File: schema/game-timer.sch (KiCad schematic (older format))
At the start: 39 parts, among them IC1 ATMEGA8515-P, SW1 Старт, SW10 Игрок4, SW2 Сброс, SW3 Время1, SW4 Время2, SW5 Время3, SW6 Время4, SW7 Игрок1, SW8 Игрок1, SW9 Игрок3

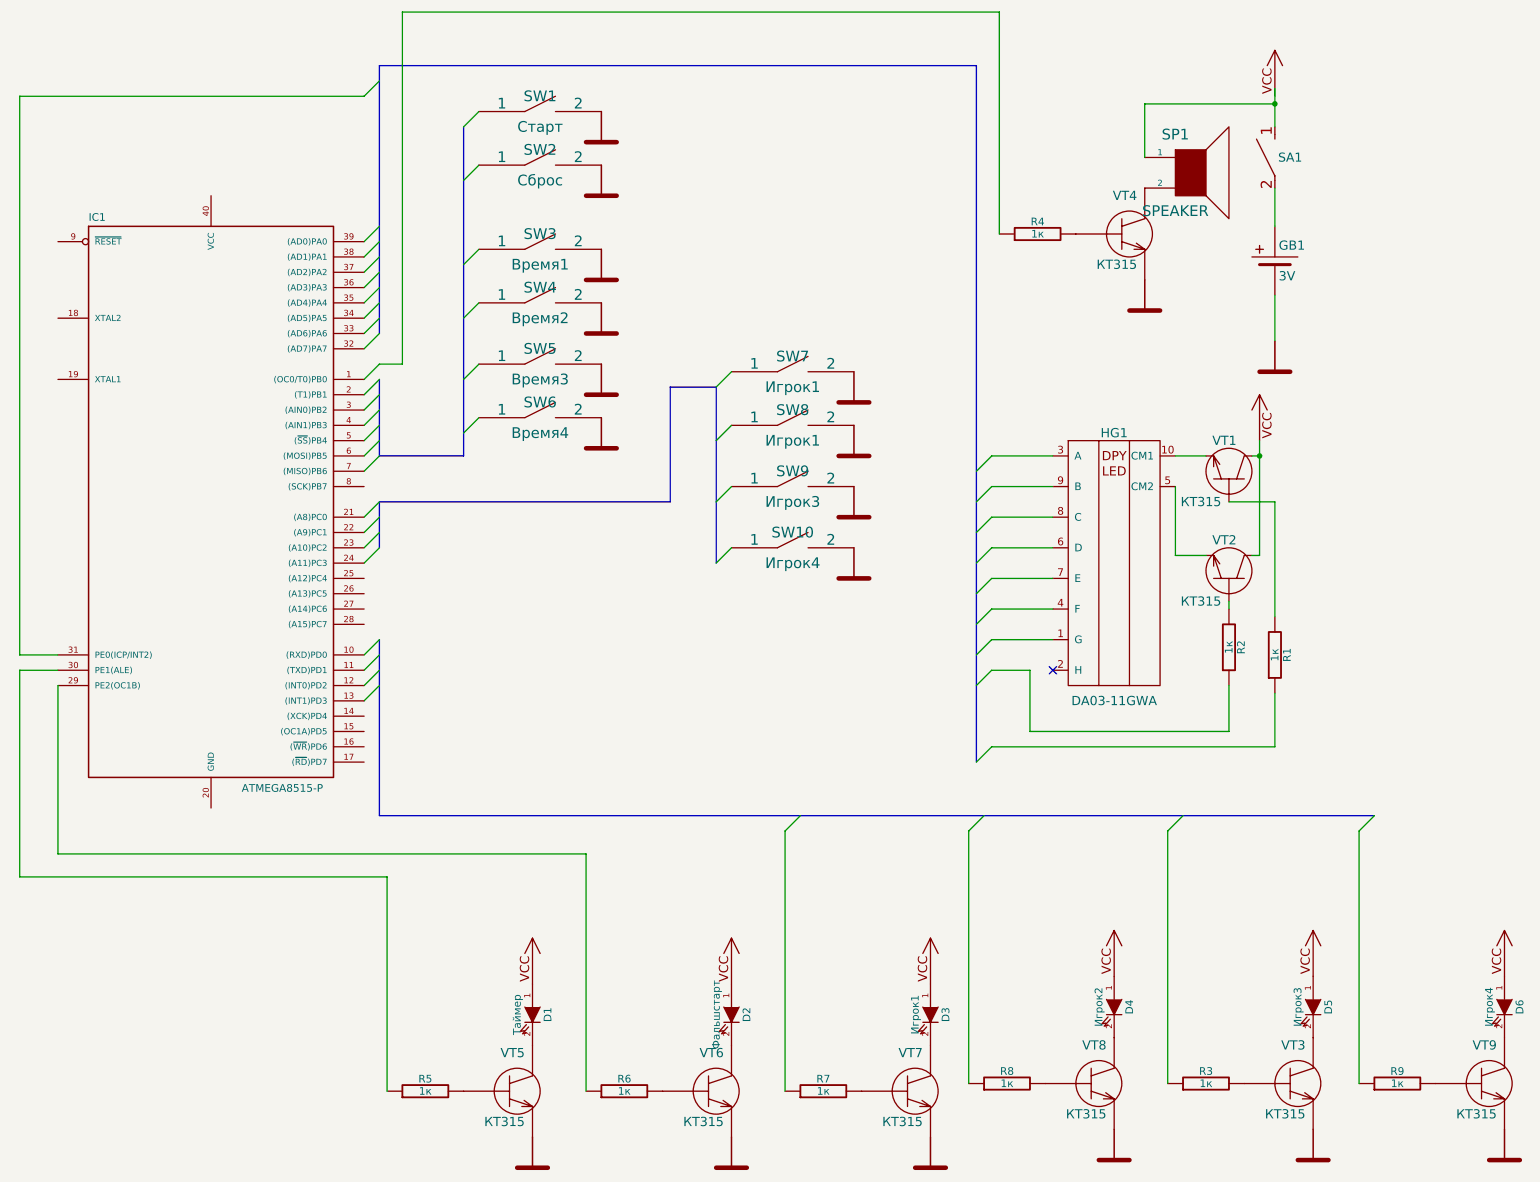
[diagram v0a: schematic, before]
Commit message: Изменена схема. Удалена динамическая индикация
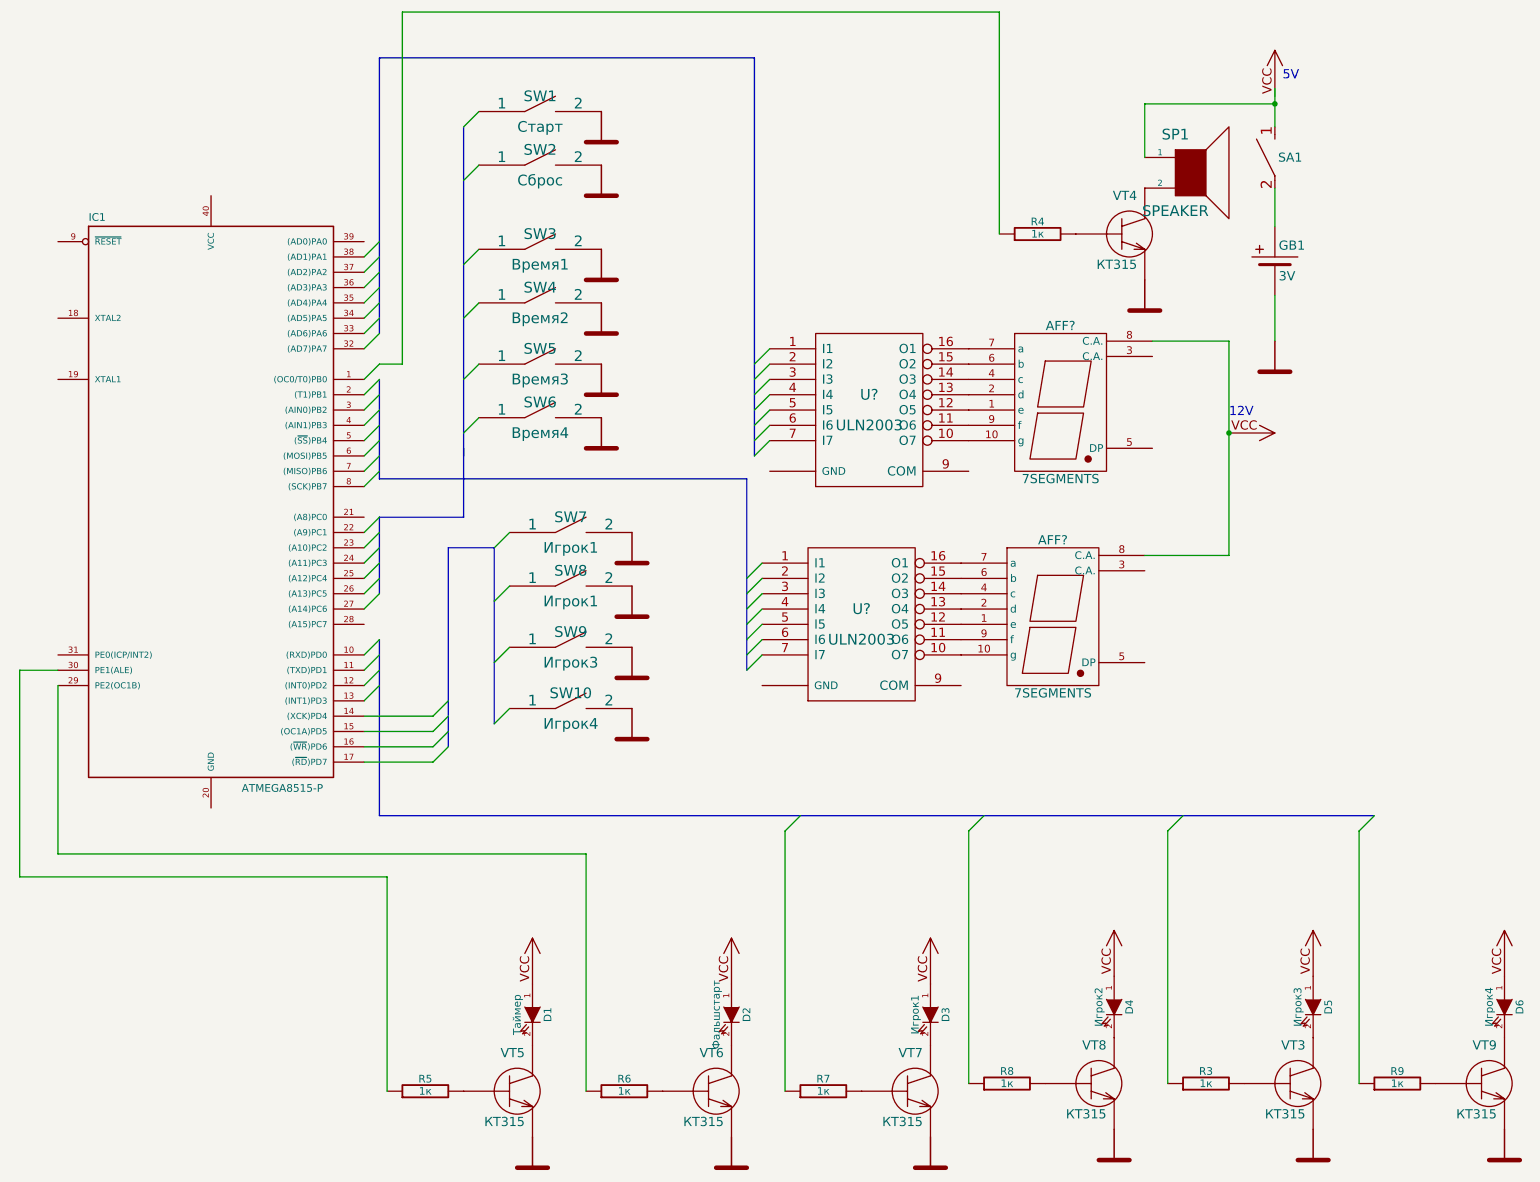
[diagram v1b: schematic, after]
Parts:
- removed HG1: DA03-11GWA, symbol HG_LED_7SEG_2_1
- removed R1, R2: 1к, symbol R
- removed VT1, VT2: КТ315, symbol VT_NPN_BCE
- added AFF? (x2): 7SEGMENTS, symbol 7SEGMENTS
- added U? (x2): ULN2003, symbol ULN2003
- added U?: POWER_VCC, symbol POWER_VCC
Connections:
- wire segments 45 -> 27
- no-connect marks 1 -> 0
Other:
- note added: "12V"
- note added: "5V"
- moved on the sheet: SW10, SW7, SW8, SW9

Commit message: Обновлена схема
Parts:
- removed GB1: 3V, symbol BAT
- removed R8, R9: 1к, symbol R
- removed SA1: SA_1-2_CL, symbol SA_1-2_CL
- removed U?: POWER_VCC, symbol POWER_VCC
- removed VT3, VT5, VT6, VT7, VT8, VT9: КТ315, symbol TR_NPN_BCE
- added R1, R2: 1к, symbol R
- added U2: ULN2003, symbol ULN2003
- gave numbers to parts that had none: 4
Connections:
- net labels added: A1, A2, B1, B2, C1, C2, D1, D2, E1, E2, F1, F2, False, G1, G2, Player1, Player2, Player3, Player4, Reset, SW1, SW2, SW3, SW4, Start, Time1, Time2, Time3, Time4, Timer
- wire segments 27 -> 90
- no-connect marks 0 -> 15
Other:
- note removed: "12V"
- note removed: "5V"
- moved on the sheet: AFF1, AFF2, D2, D3, D4, D5, D6, R4, R5, SP1, SW1, SW10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
